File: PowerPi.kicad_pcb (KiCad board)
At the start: 2 copper layers, 65 x 56 mm, 34 parts, among them J1 2444, J3 Conn_01x02, J6 Raspberry_Pi_2_3, J8 2444, Q1 30V 4A 44mΩ, Q2 50nA 150V 200mW 200mA, Q3 30V 4A 44mΩ, U1 XL4015

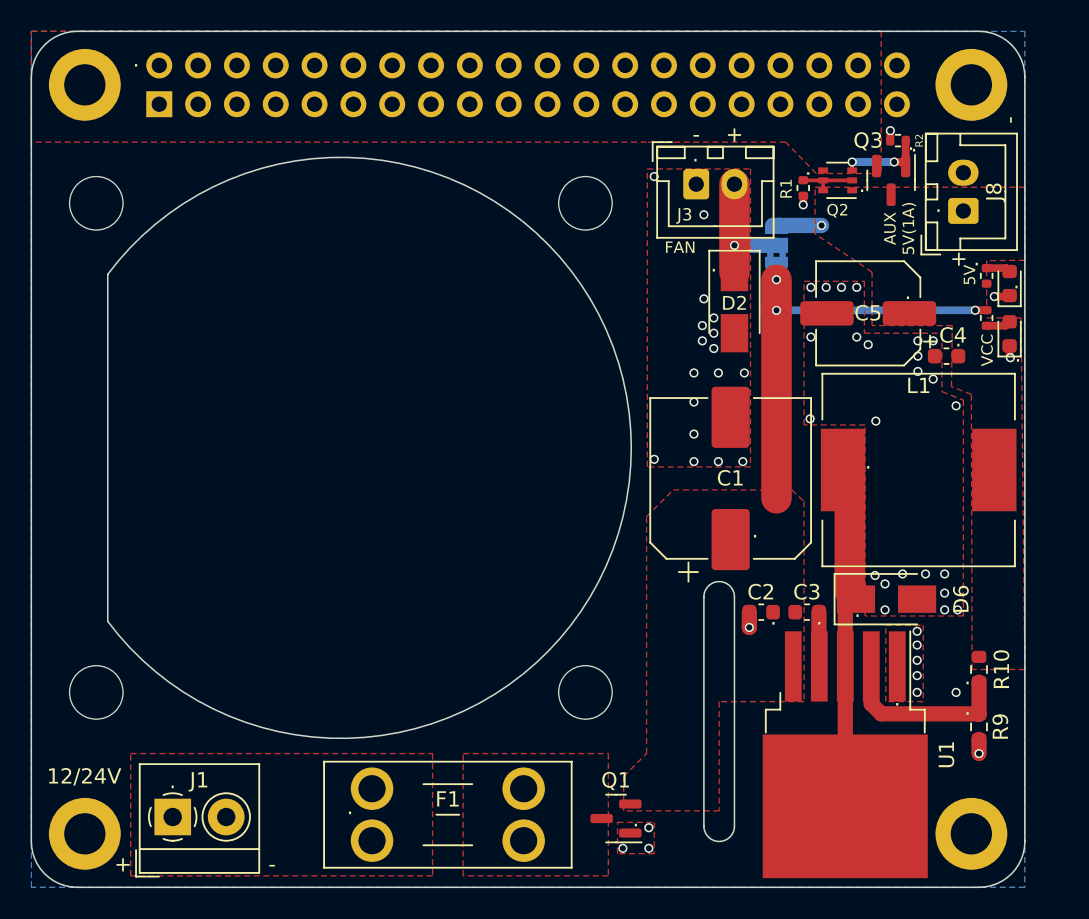
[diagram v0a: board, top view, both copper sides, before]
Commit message: changed input capacitors to 0402 footprint and updated layout to reduce EMI
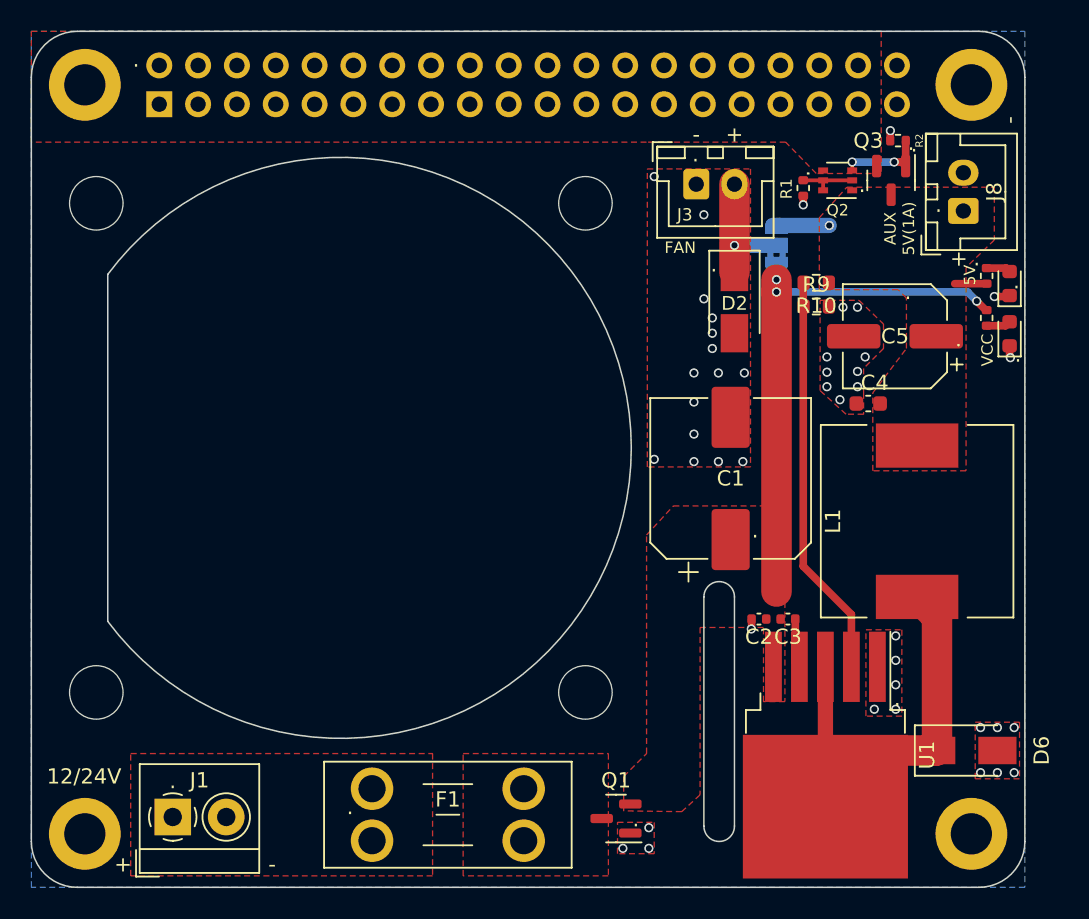
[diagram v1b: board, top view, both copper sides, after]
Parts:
- C2, C3: footprint Capacitor_SMD:C_0603_1608Metric -> Capacitor_SMD:C_0402_1005Metric
- moved R9 29.5 mm to (136.6, 71.2), turned to 0 degrees
- moved R10 27.5 mm to (136.6, 69.7), turned to 0 degrees
- moved D6 11.2 mm to (146.4, 100.3)
- moved C4 5.99 mm to (140.0, 77.6)
- moved L1 3.35 mm to (143.2, 85.3), turned to 90 degrees
- moved C5 2.30 mm to (141.8, 73.2)
- moved C3 1.33 mm to (134.8, 91.7)
- moved U1 1.30 mm to (137.2, 100.6)
- moved C2 0.47 mm to (132.8, 91.7)
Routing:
- net Net-(R10-Pad1): track 12.0 -> 26.4 mm
- net VCC: track 29.0 -> 35.6 mm
- net Net-(D6-Pad1): track 22.4 -> 28.5 mm
- net +5V: track 2.95 -> 5.54 mm
- net GND: track 4.99 -> 3.64 mm, vias 56 -> 43

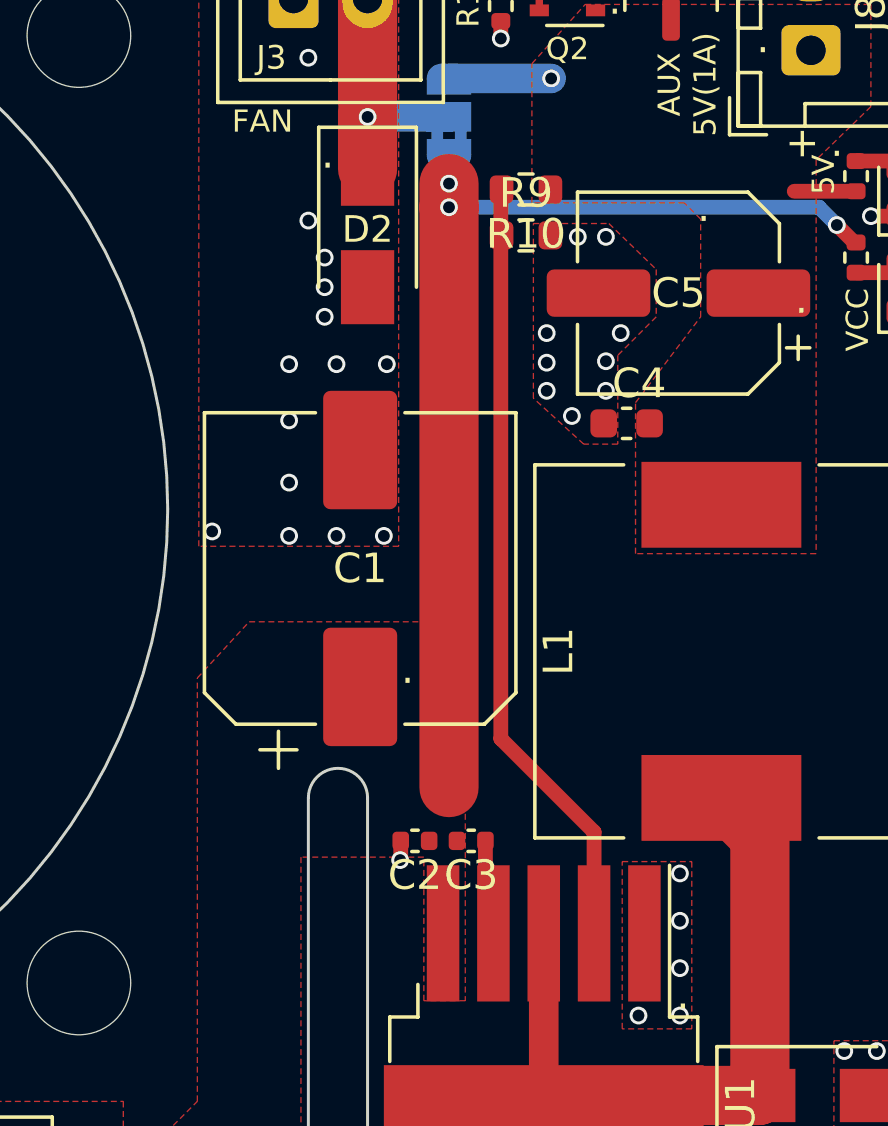
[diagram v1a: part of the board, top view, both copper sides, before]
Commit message: improved copper balance
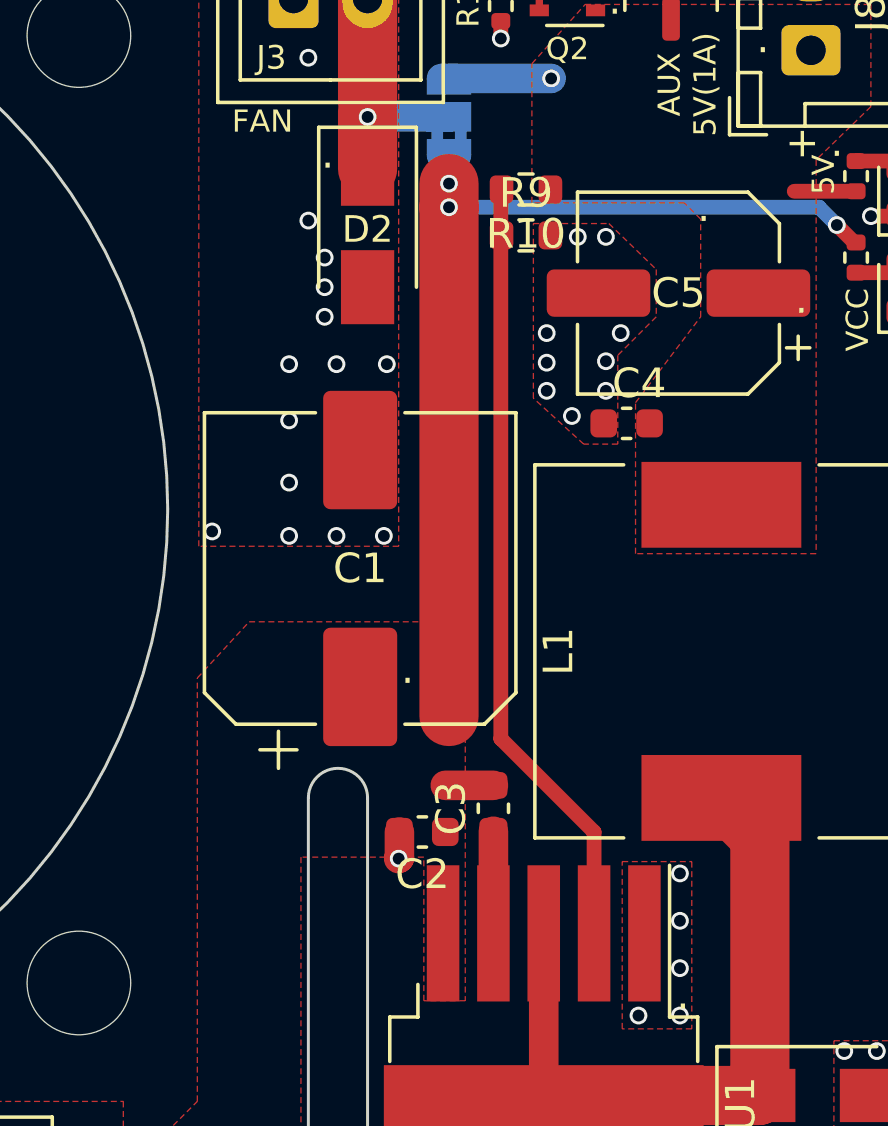
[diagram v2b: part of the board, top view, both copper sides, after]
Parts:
- C2, C3: footprint Capacitor_SMD:C_0402_1005Metric -> Capacitor_SMD:C_0603_1608Metric
- moved C3 1.33 mm to (135.5, 90.6), turned to 90 degrees
- moved C2 0.39 mm to (133.1, 91.4)
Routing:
- net VCC: track 35.6 -> 34.8 mm

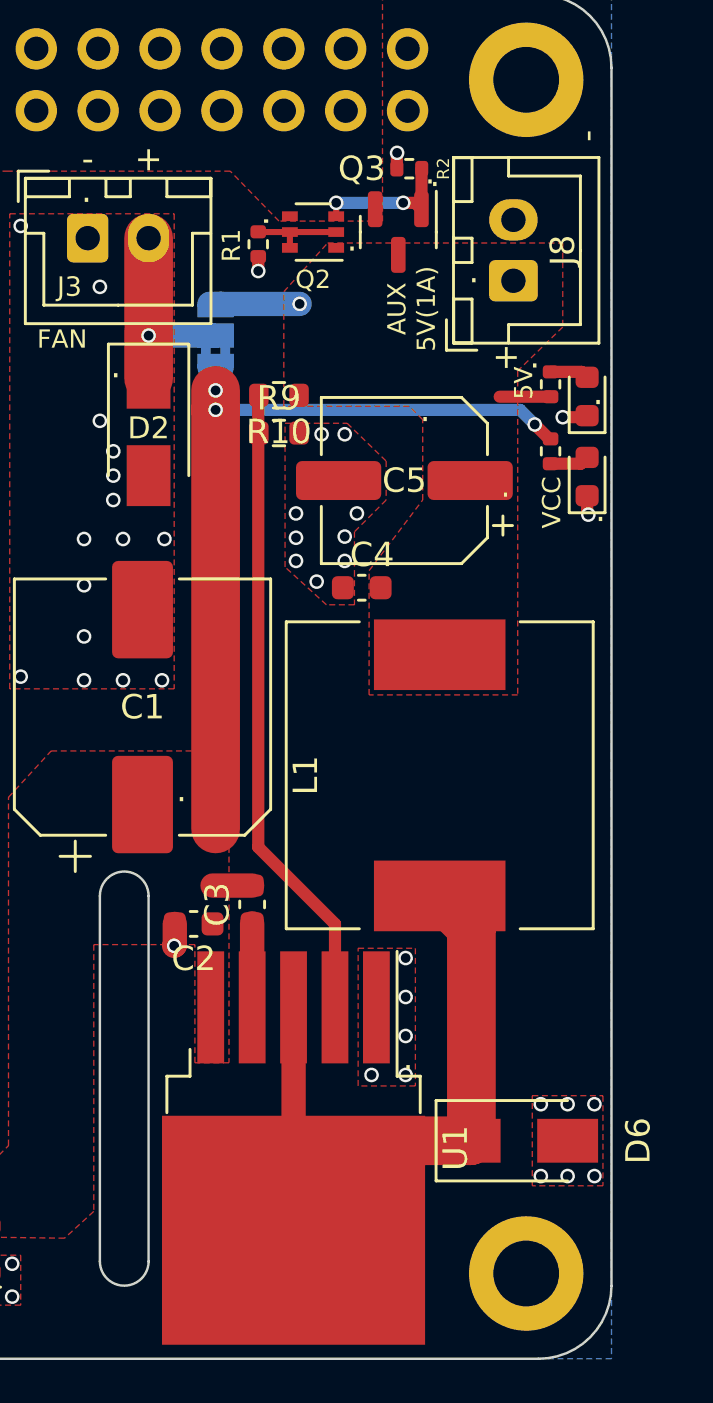
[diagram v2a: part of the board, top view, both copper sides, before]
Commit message: update to 1000 uF output electrolytic capacitor
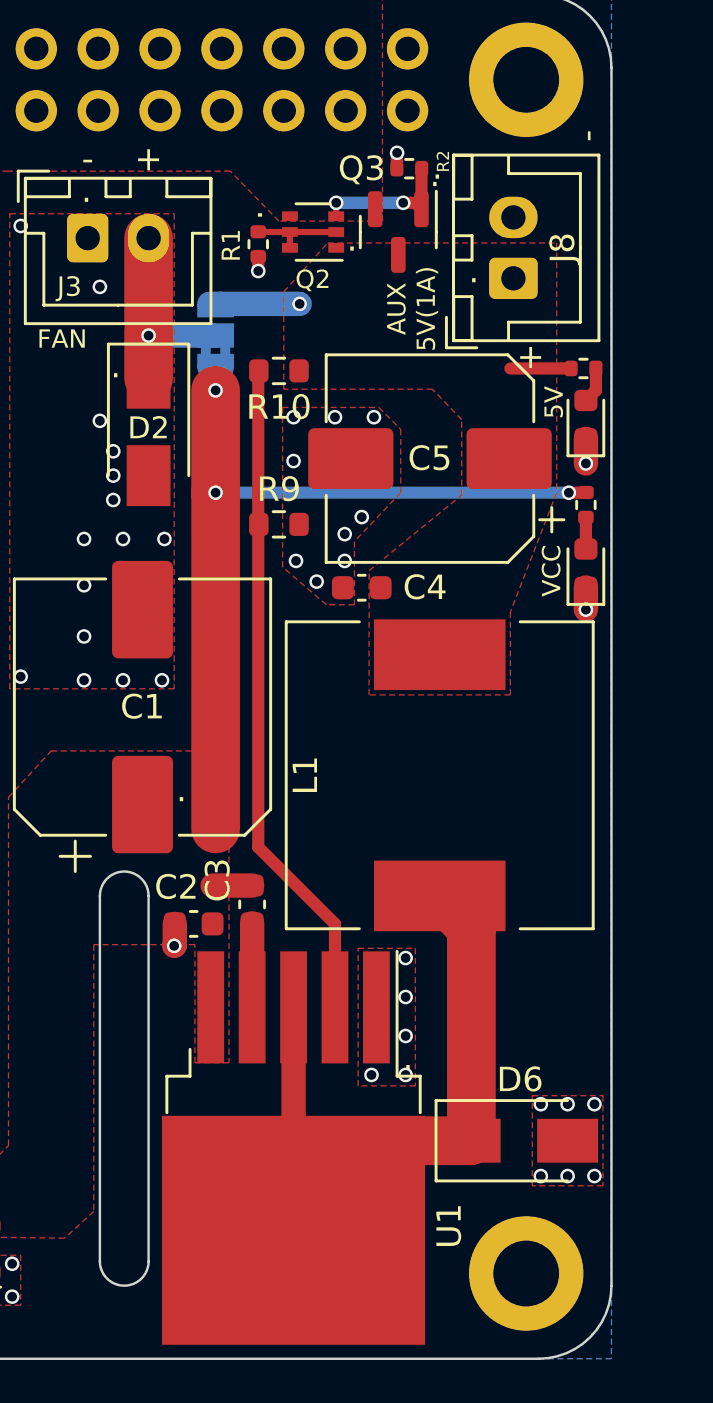
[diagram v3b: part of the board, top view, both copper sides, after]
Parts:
- C5: value 330uF -> 1000uF; footprint Capacitor_SMD:CP_Elec_6.3x7.7 -> Capacitor_SMD:CP_Elec_8x10
- moved D5 3.76 mm to (149.2, 76.8)
- moved R9 3.75 mm to (136.6, 75.0)
- moved R8 2.63 mm to (149.2, 74.2)
- moved R6 1.50 mm to (149.1, 68.6), turned to 180 degrees
- moved C5 1.38 mm to (142.8, 72.3)
- moved R10 1.00 mm to (136.6, 68.7)
- moved D3 0.95 mm to (149.2, 70.7)
- moved J8 0.10 mm to (146.2, 64.9)
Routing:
- net Net-(R10-Pad1): track 26.4 -> 27.4 mm
- net VCC: track 34.8 -> 35.8 mm
